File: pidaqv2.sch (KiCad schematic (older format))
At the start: 9 parts, among them J101 Screw_Terminal_01x10, J102 Screw_Terminal_01x06, J103 Conn_01x02_Male, J104 Screw_Terminal_01x04, J105 Screw_Terminal_01x08, U1 RASPBERRY_PI_3_MODEL_B+

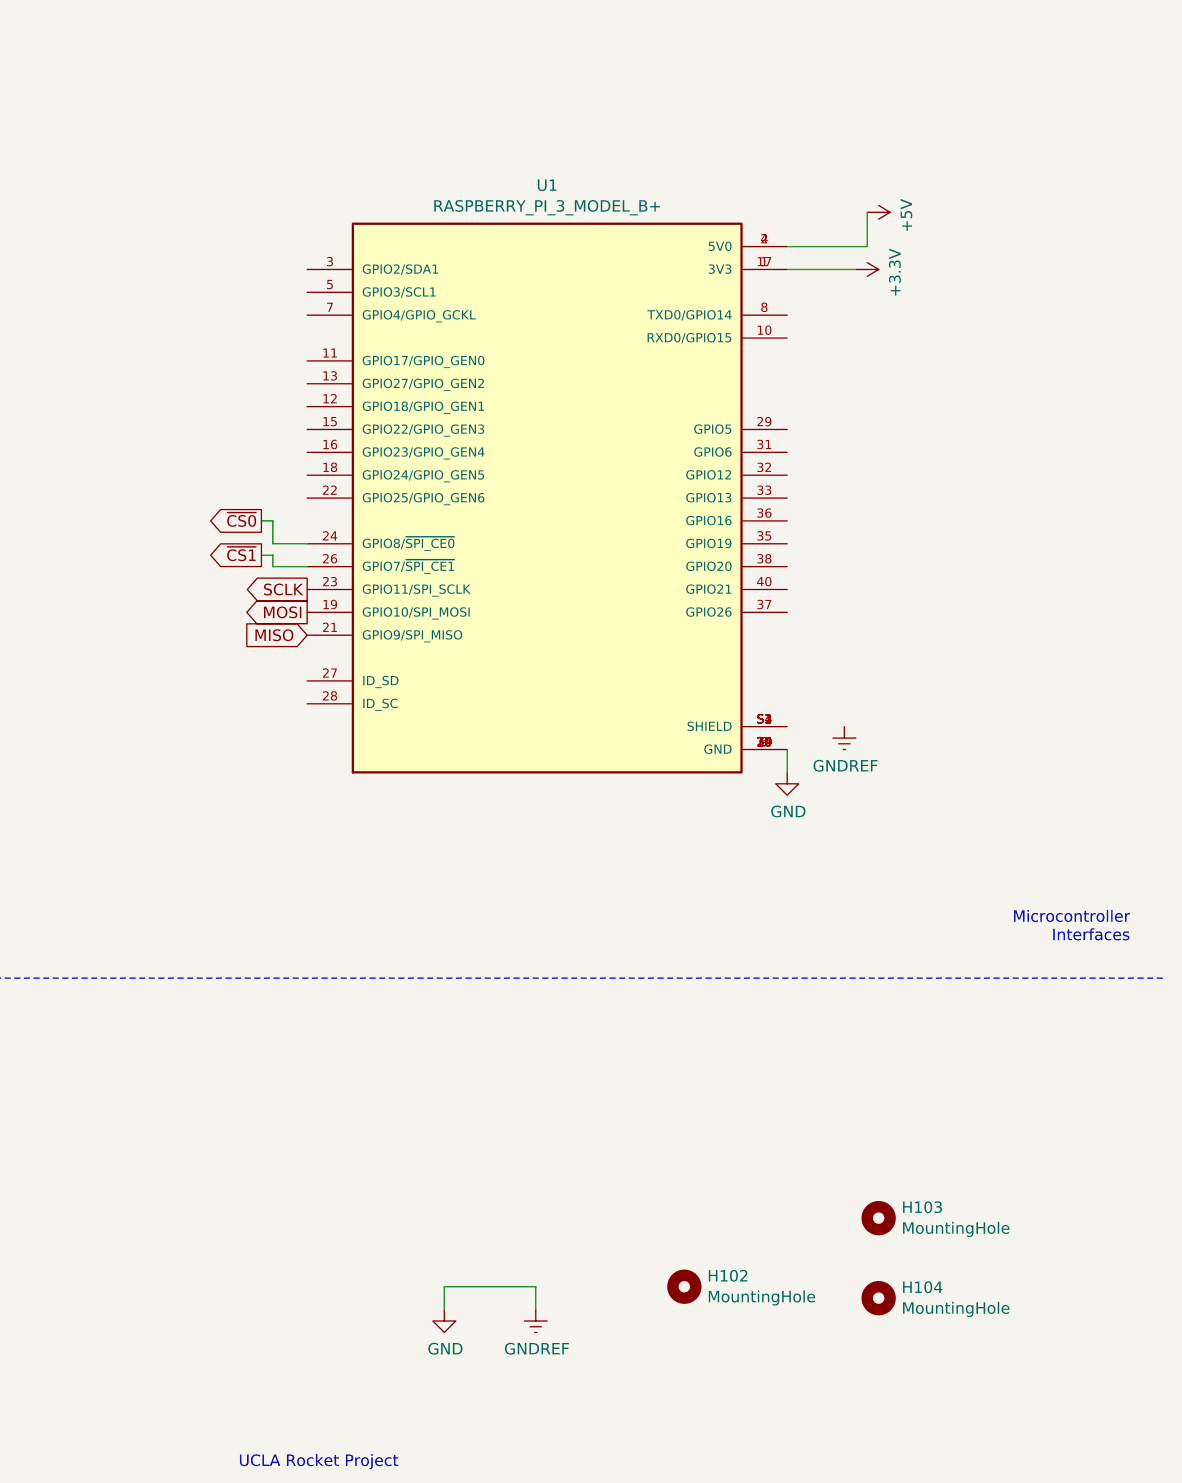
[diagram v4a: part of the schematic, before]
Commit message: slid the header to the right, and set IO to 3.3V
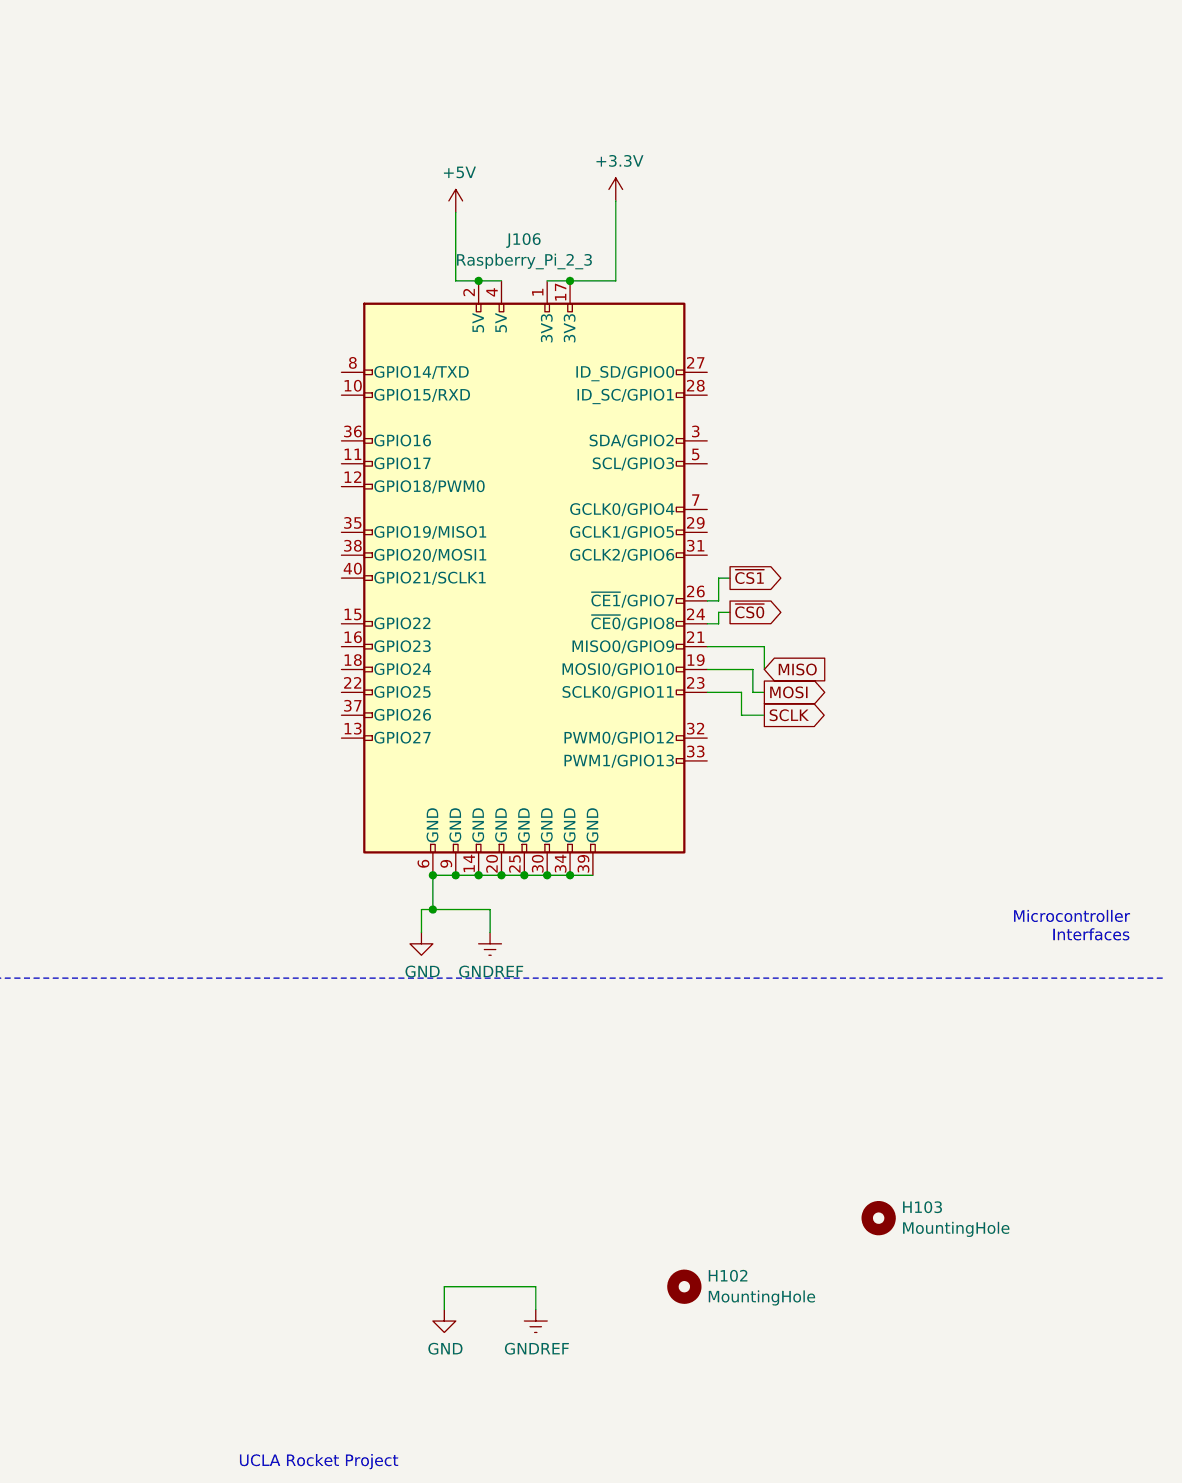
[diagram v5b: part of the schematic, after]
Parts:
- removed H104: MountingHole, MountingHole:MountingHole_3.2mm_M3_ISO7380, symbol Mechanical:MountingHole
- removed U1: RASPBERRY_PI_3_MODEL_B+, MODULE_RASPBERRY_PI_3_MODEL_B+, symbol RASPBERRY_PI_3_MODEL_B_:RASPBERRY_PI_3_MODEL_B+
- added J106: Raspberry_Pi_2_3, Connector_PinHeader_2.54mm:PinHeader_2x20_P2.54mm_Vertical, symbol Connector:Raspberry_Pi_2_3
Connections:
- net +3V3: now also J106.1 (3V3), J106.17 (3V3)
- net +5V: now also J106.2 (5V), J106.4 (5V)
- net GND: now also J106.14 (GND), J106.20 (GND), J106.25 (GND), J106.30 (GND), J106.34 (GND), J106.39 (GND), J106.6 (GND), J106.9 (GND)
- net MISO: now also J106.21 (MISO0/GPIO9)
- net MOSI: now also J106.19 (MOSI0/GPIO10)
- net SCLK: now also J106.23 (SCLK0/GPIO11)
- net ~CS0: now also J106.24 (~CE0~/GPIO8)
- net ~CS1: now also J106.26 (~CE1~/GPIO7)
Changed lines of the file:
@@
-$EndComp
-$Comp
-L Mechanical:MountingHole H104
-U 1 1 5F4F092C
-P 9950 6100
-F 0 "H104" H 10050 6146 50  0000 L CNN
-F 1 "MountingHole" H 10050 6055 50  0000 L CNN
-F 2 "MountingHole:MountingHole_3.2mm_M3_ISO7380" H 9950 6100 50  0001 C CNN
-F 3 "~" H 9950 6100 50  0001 C CNN
-	1    9950 6100
-	1    0    0    -1
 $EndComp
 $Comp
@@
 L power:+3.3V #PWR0101
 U 1 1 5F6A340B
-P 9850 1600
-F 0 "#PWR0101" H 9850 1450 50  0001 C CNN
-F 1 "+3.3V" H 9865 1773 50  0000 C CNN
-F 2 "" H 9850 1600 50  0001 C CNN
-F 3 "" H 9850 1600 50  0001 C CNN
-	1    9850 1600
-	0    1    1    0
-$EndComp
-Wire Wire Line
-	9550 1600 9850 1600
+P 8800 1300
+F 0 "#PWR0101" H 8800 1150 50  0001 C CNN
+F 1 "+3.3V" H 8815 1473 50  0000 C CNN
+F 2 "" H 8800 1300 50  0001 C CNN
+F 3 "" H 8800 1300 50  0001 C CNN
+	1    8800 1300
+	1    0    0    -1
+$EndComp
 $Comp
 L power:GND #PWR0103
 U 1 1 5F6AA8DA
-P 9550 3800
-F 0 "#PWR0103" H 9550 3550 50  0001 C CNN
-F 1 "GND" H 9555 3627 50  0000 C CNN
-F 2 "" H 9550 3800 50  0001 C CNN
-F 3 "" H 9550 3800 50  0001 C CNN
-	1    9550 3800
-	1    0    0    -1
-$EndComp
-Text GLabel 7450 3000 0    50   Output ~ 0
+P 7950 4500
+F 0 "#PWR0103" H 7950 4250 50  0001 C CNN
+F 1 "GND" H 7955 4327 50  0000 C CNN
+F 2 "" H 7950 4500 50  0001 C CNN
+F 3 "" H 7950 4500 50  0001 C CNN
+	1    7950 4500
+	1    0    0    -1
+$EndComp
+Text GLabel 9450 3550 2    50   Output ~ 0
 SCLK
-Text GLabel 7450 3200 0    50   Input ~ 0
+Text GLabel 9450 3350 2    50   Input ~ 0
 MISO
-Text GLabel 7450 3100 0    50   Output ~ 0
+Text GLabel 9450 3450 2    50   Output ~ 0
 MOSI
-Wire Wire Line
-	7450 2900 7300 2900
-Wire Wire Line
-	7300 2900 7300 2850
-Wire Wire Line
-	7450 2800 7300 2800
-Wire Wire Line
-	7300 2800 7300 2700
-Wire Wire Line
-	7300 2700 7250 2700
 Wire Wire Line
 	2500 3300 2600 3300
@@
 NoConn ~ 2850 6550
 Wire Wire Line
-	9550 3700 9550 3800
+	7950 4400 7950 4500
 $Comp
 L power:GNDREF #PWR0138
 U 1 1 5F7D69C3
-P 9800 3600
-F 0 "#PWR0138" H 9800 3350 50  0001 C CNN
-F 1 "GNDREF" H 9805 3427 50  0000 C CNN
-F 2 "" H 9800 3600 50  0001 C CNN
-F 3 "" H 9800 3600 50  0001 C CNN
-	1    9800 3600
+P 8250 4500
+F 0 "#PWR0138" H 8250 4250 50  0001 C CNN
+F 1 "GNDREF" H 8255 4327 50  0000 C CNN
+F 2 "" H 8250 4500 50  0001 C CNN
+F 3 "" H 8250 4500 50  0001 C CNN
+	1    8250 4500
 	1    0    0    -1
 $EndComp
@@
 Wire Wire Line
 	1700 1300 2850 1300
-$Comp
-L RASPBERRY_PI_3_MODEL_B_:RASPBERRY_PI_3_MODEL_B+ U1
-U 1 1 5FC69FBF
-P 8550 2400
-F 0 "U1" H 8500 3567 50  0000 C CNN
-F 1 "RASPBERRY_PI_3_MODEL_B+" H 8500 3476 50  0000 C CNN
-F 2 "MODULE_RASPBERRY_PI_3_MODEL_B+" H 8550 2400 50  0001 L BNN
-F 3 "" H 8550 2400 50  0001 L BNN
-F 4 "Manufacturer Recommendations" H 8550 2400 50  0001 L BNN "STANDARD"
-F 5 "18mm" H 8550 2400 50  0001 L BNN "MAXIMUM_PACKAGE_HIEGHT"
-F 6 "1.0" H 8550 2400 50  0001 L BNN "PARTREV"
-F 7 "Raspberry Pi" H 8550 2400 50  0001 L BNN "MANUFACTURER"
-	1    8550 2400
-	1    0    0    -1
-$EndComp
-Text GLabel 7250 2700 0    50   Output ~ 0
+Text GLabel 9300 3100 2    50   Output ~ 0
 ~CS0
 Wire Wire Line
-	7300 2850 7250 2850
-Text GLabel 7250 2850 0    50   Output ~ 0
+	9250 2950 9300 2950
+Text GLabel 9300 2950 2    50   Output ~ 0
 ~CS1
-Wire Wire Line
-	9900 1500 9550 1500
-Wire Wire Line
-	9900 1350 9900 1500
 $Comp
 L power:+5V #PWR0102
 U 1 1 5F6A5CF8
-P 9900 1350
-F 0 "#PWR0102" H 9900 1200 50  0001 C CNN
-F 1 "+5V" H 9915 1523 50  0000 C CNN
-F 2 "" H 9900 1350 50  0001 C CNN
-F 3 "" H 9900 1350 50  0001 C CNN
-	1    9900 1350
-	0    1    1    0
-$EndComp
+P 8100 1350
+F 0 "#PWR0102" H 8100 1200 50  0001 C CNN
+F 1 "+5V" H 8115 1523 50  0000 C CNN
+F 2 "" H 8100 1350 50  0001 C CNN
+F 3 "" H 8100 1350 50  0001 C CNN
+	1    8100 1350
+	1    0    0    -1
+$EndComp
+$Comp
+L Connector:Raspberry_Pi_2_3 J106
+U 1 1 5FCA078E
+P 8400 2950
+F 0 "J106" H 8400 4431 50  0000 C CNN
+F 1 "Raspberry_Pi_2_3" H 8400 4340 50  0000 C CNN
+F 2 "Connector_PinHeader_2.54mm:PinHeader_2x20_P2.54mm_Vertical" H 8400 2950 50  0001 C CNN
+F 3 "https://www.raspberrypi.org/documentation/hardware/raspberrypi/schematics/rpi_SCH_3bplus_1p0_reduced.pdf" H 8400 2950 50  0001 C CNN
+	1    8400 2950
+	1    0    0    -1
+$EndComp
+Wire Wire Line
+	9250 2950 9250 3050
+Wire Wire Line
+	9250 3050 9200 3050
+Wire Wire Line
+	8250 4400 8250 4500
+Wire Wire Line
+	7950 4400 8000 4400
+Wire Wire Line
+	8700 4250 8600 4250
+Connection ~ 8100 4250
+Wire Wire Line
+	8100 4250 8000 4250
+Connection ~ 8200 4250
+Wire Wire Line
+	8200 4250 8100 4250
+Connection ~ 8300 4250
+Wire Wire Line
+	8300 4250 8200 4250
+Connection ~ 8400 4250
+Wire Wire Line
+	8400 4250 8300 4250
+Connection ~ 8500 4250
+Wire Wire Line
+	8500 4250 8400 4250
+Connection ~ 8600 4250
+Wire Wire Line
+	8600 4250 8500 4250
+Wire Wire Line
+	8000 4250 8000 4400
+Connection ~ 8000 4250
+Connection ~ 8000 4400
+Wire Wire Line
+	8000 4400 8250 4400
+Wire Wire Line
+	8300 1650 8200 1650
+Wire Wire Line
+	8100 1650 8100 1350
+Connection ~ 8200 1650
+Wire Wire Line
+	8200 1650 8100 1650
+Wire Wire Line
+	8800 1300 8800 1650
+Wire Wire Line
+	8800 1650 8600 1650
+Connection ~ 8600 1650
+Wire Wire Line
+	8600 1650 8500 1650
+Wire Wire Line
+	9300 3100 9250 3100
+Wire Wire Line
+	9250 3100 9250 3150
+Wire Wire Line
+	9250 3150 9200 3150
+Wire Wire Line
+	9450 3350 9450 3250
+Wire Wire Line
+	9450 3250 9200 3250
+Wire Wire Line
+	9450 3450 9400 3450
+Wire Wire Line
+	9400 3450 9400 3350
+Wire Wire Line
+	9400 3350 9200 3350
+Wire Wire Line
+	9450 3550 9350 3550
+Wire Wire Line
+	9350 3550 9350 3450
+Wire Wire Line
+	9350 3450 9200 3450
 $EndSCHEMATC
